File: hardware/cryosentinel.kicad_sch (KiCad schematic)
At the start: 42 parts, among them J1 USB-C-16P, J2 JST-PH-2, J3 U.FL LoRa Antenna, J4 U.FL GPS Antenna, Q1 MMBT2222, U1 ESP32-C3-MINI-1, U10 1.54in e-ink FPC-8, U11 AT25DF321, U2 SHT40, U3 ATECC608A, U4 ST25DV04K, U5 ADXL345, U6 SX1262, U7 MAX-M10S, U8 MAX17048, U9 TP4056

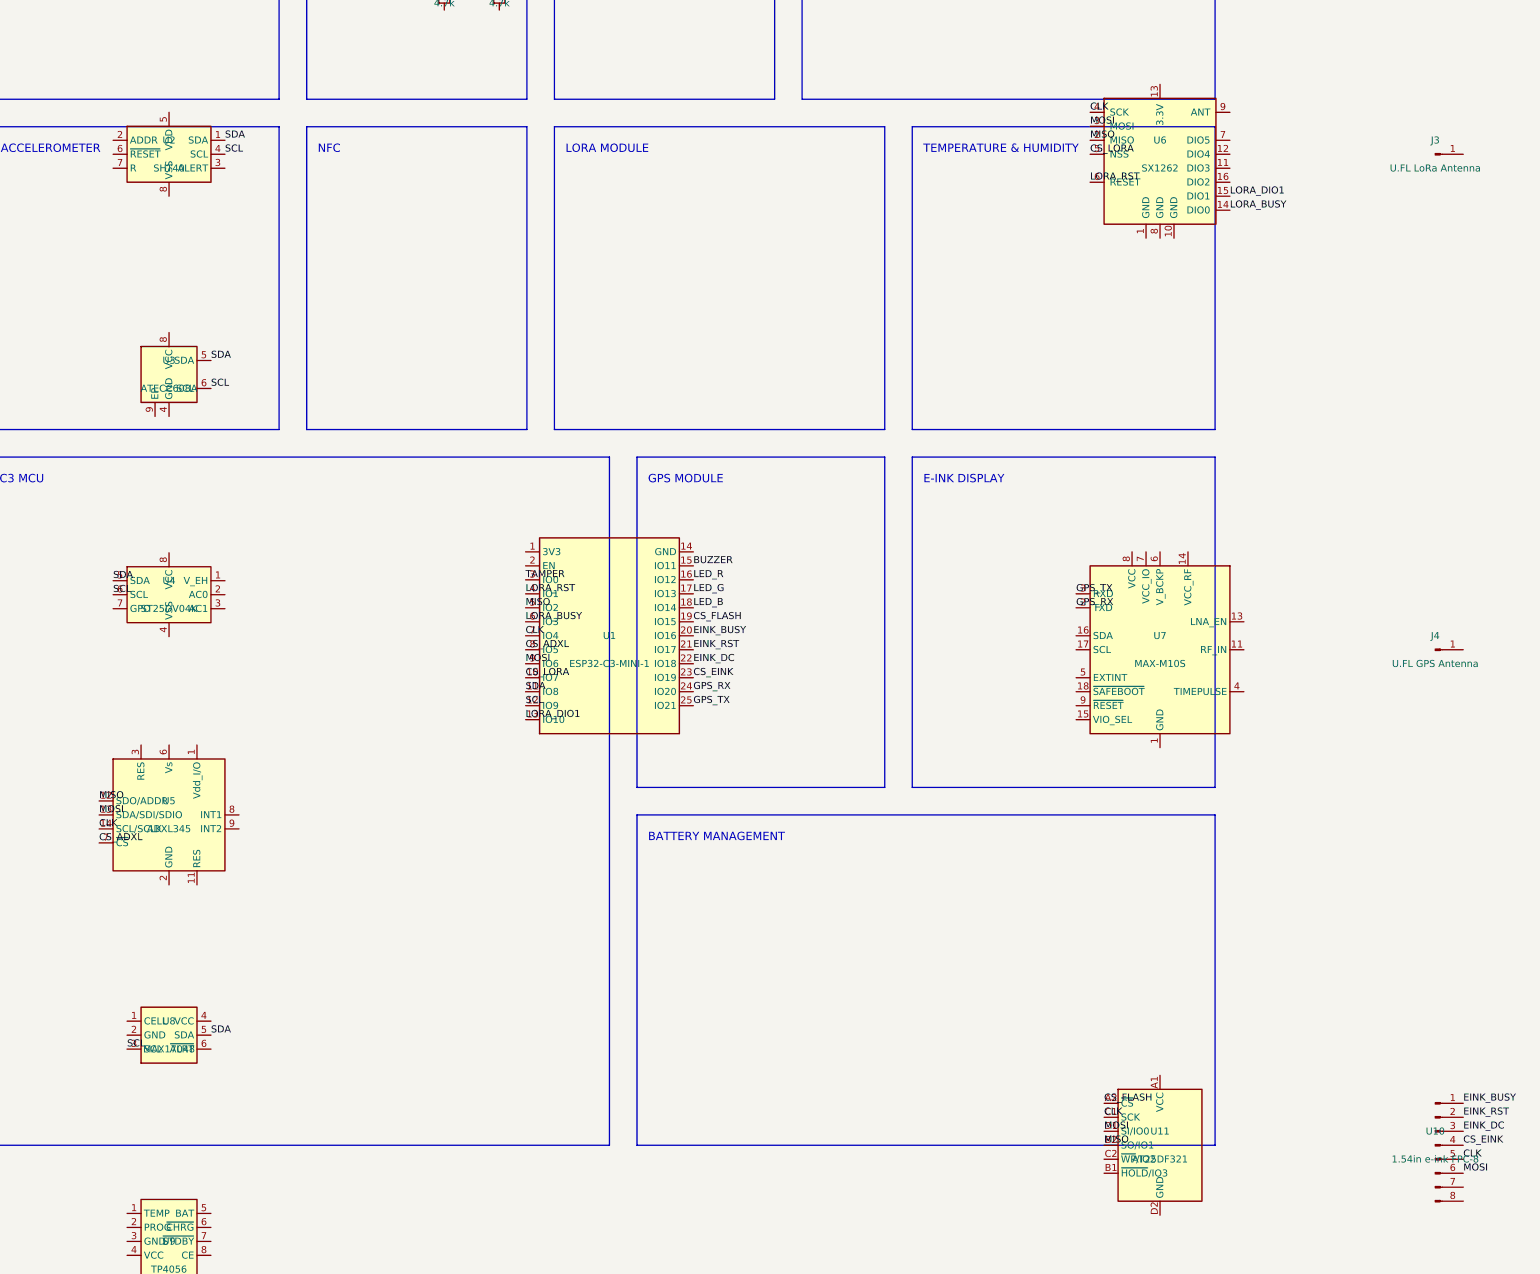
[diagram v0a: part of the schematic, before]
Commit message: fix: Generate true side-by-side schematic with passives and break cache
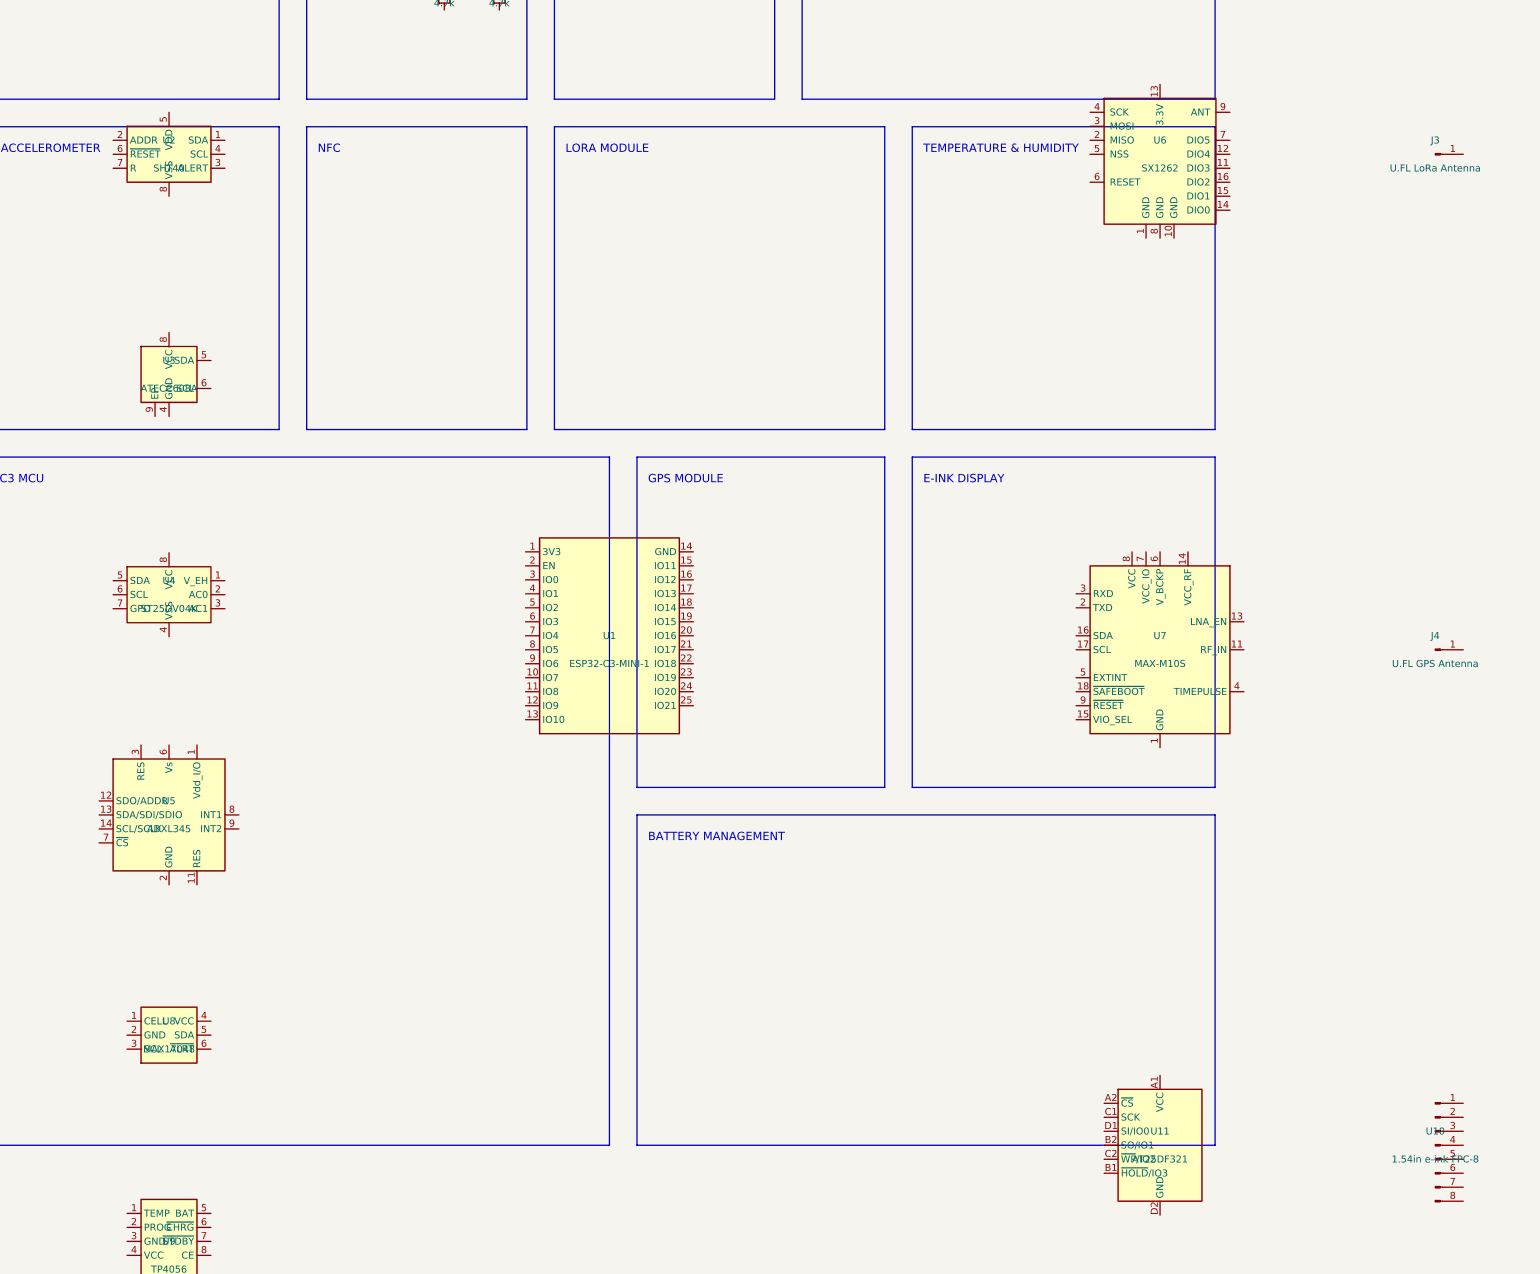
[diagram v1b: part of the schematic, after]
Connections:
- net BUZZER: no longer names the net of U1.15 (IO11)
- removed net CLK: U1.7 (IO4), U10.5 (Pin_5), U11.C1 (SCK), U5.14 (SCL/SCLK), U6.4 (SCK)
- net CS_ADXL: no longer names the net of U1.8 (IO5)
- net CS_ADXL: no longer U5.7 (~{CS})
- net CS_EINK: no longer names the net of U1.23 (IO19)
- net CS_EINK: no longer U10.4 (Pin_4)
- net CS_FLASH: no longer names the net of U1.19 (IO15)
- net CS_FLASH: no longer U11.A2 (~{CS})
- net CS_LORA: no longer names the net of U1.10 (IO7)
- net CS_LORA: no longer U6.5 (NSS)
- net EINK_BUSY: no longer names the net of U1.20 (IO16)
- net EINK_BUSY: no longer U10.1 (Pin_1)
- net EINK_DC: no longer names the net of U1.22 (IO18)
- net EINK_DC: no longer U10.3 (Pin_3)
- net EINK_RST: no longer names the net of U1.21 (IO17)
- net EINK_RST: no longer U10.2 (Pin_2)
- net GPS_RX: no longer names the net of U1.24 (IO20)
- net GPS_RX: no longer U7.2 (TXD)
- net GPS_TX: no longer names the net of U1.25 (IO21)
- net GPS_TX: no longer U7.3 (RXD)
- net LED_B: no longer names the net of U1.18 (IO14)
- net LED_G: no longer names the net of U1.17 (IO13)
- net LED_R: no longer names the net of U1.16 (IO12)
- net LORA_BUSY: no longer names the net of U1.6 (IO3)
- net LORA_BUSY: no longer U6.14 (DIO0)
- net LORA_DIO1: no longer names the net of U1.13 (IO10)
- net LORA_DIO1: no longer U6.15 (DIO1)
- net LORA_RST: no longer names the net of U1.4 (IO1)
- net LORA_RST: no longer U6.6 (RESET)
- removed net MISO: U1.5 (IO2), U11.B2 (SO/IO1), U5.12 (SDO/ADDR), U6.2 (MISO)
- removed net MOSI: U1.9 (IO6), U10.6 (Pin_6), U11.D1 (SI/IO0), U5.13 (SDA/SDI/SDIO), U6.3 (MOSI)
- removed net SCL: U1.12 (IO9), U2.4 (SCL), U3.6 (SCL), U4.6 (SCL), U8.3 (SCL)
- removed net SDA: U1.11 (IO8), U2.1 (SDA), U3.5 (SDA), U4.5 (SDA), U8.5 (SDA)
- net TAMPER: no longer names the net of U1.3 (IO0)
